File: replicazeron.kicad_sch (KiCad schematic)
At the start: 75 parts, among them J1 Conn_01x06_Male, J10 Conn_01x03_Pin, J2 Conn_01x06_Male, J3 Conn_01x06_Male, J4 Conn_01x06_Male, J5 Conn_01x06_Male, J6 Conn_01x05_Male, J7 Conn_01x05_Female, J8 Conn_01x06_Female, J9 Conn_01x04_Male, SW1 SW_Push, SW10 SW_Push, SW11 SW_Push, SW12 SW_Push, SW13 SW_Push, SW14 SW_Push, SW15 SW_Push, SW16 SW_Push, SW17 SW_Push, SW18 SW_Push, SW19 SW_Push, SW2 SW_Push, SW20 SW_Push, SW21 SW_Push, SW22 SW_Push, SW23 SW_Push, SW24 SW_Push, SW25 SW_Push, SW26 SW_Push, SW27 SW_Push, SW28 SW_Push, SW29 SW_Push, SW3 SW_Push, SW4 SW_Push, SW5 SW_Push, SW6 SW_Push, SW7 SW_Push, SW8 SW_Push, SW9 SW_Push, U1 STM32F103C8Tx

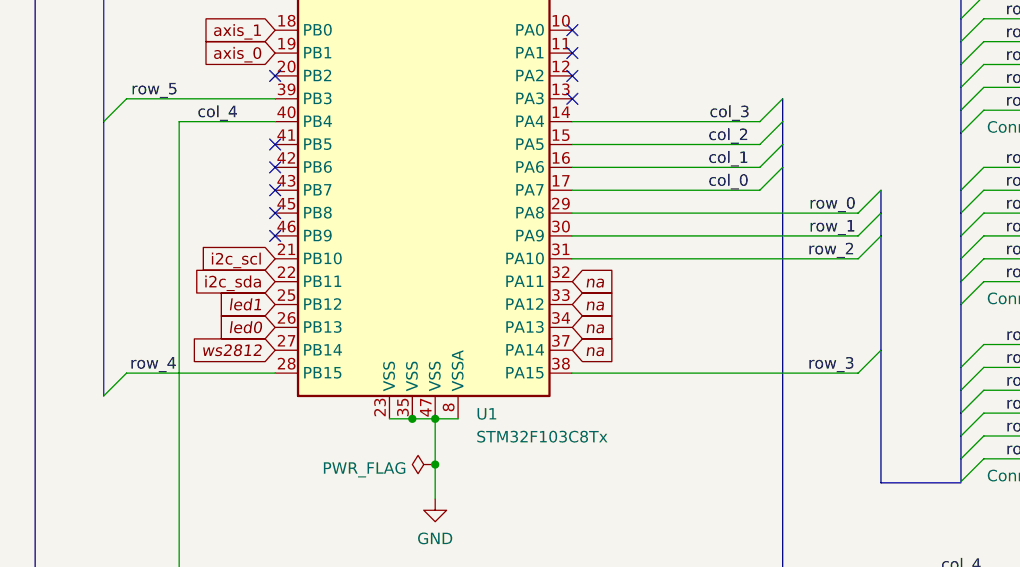
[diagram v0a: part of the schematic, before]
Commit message: fix row order
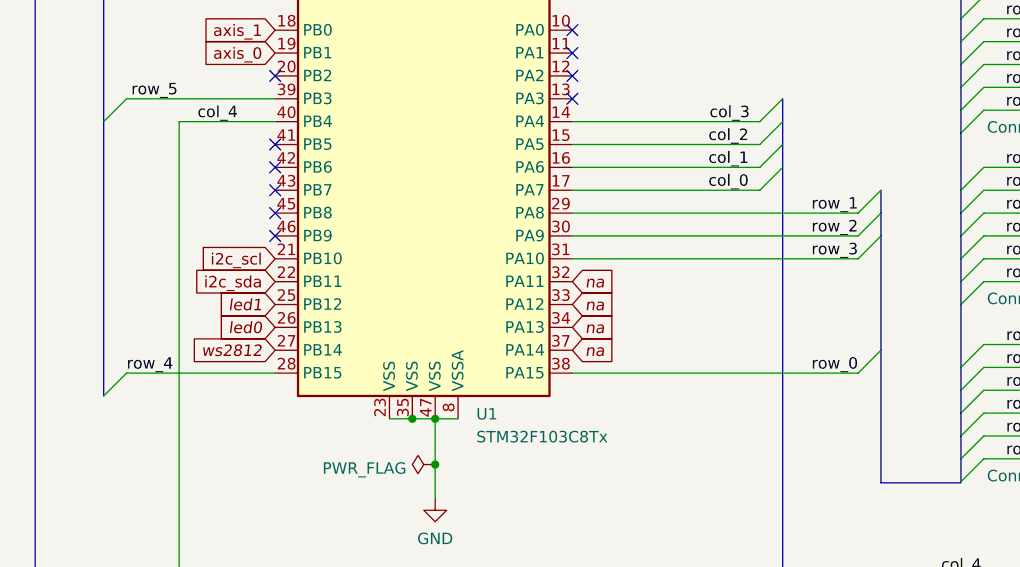
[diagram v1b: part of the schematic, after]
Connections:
- net row_0: now also U1.38 (PA15); no longer U1.29 (PA8)
- net row_1: now also U1.29 (PA8); no longer U1.30 (PA9)
- net row_2: now also U1.30 (PA9); no longer U1.31 (PA10)
- net row_3: now also U1.31 (PA10); no longer U1.38 (PA15)
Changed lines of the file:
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@@
 	)
 	(label "row_3"
-		(at 108.839 241.3 180)
+		(at 109.22 228.6 180)
 		(fields_autoplaced yes)
 		(effects
@@
 	)
 	(label "row_0"
-		(at 108.966 223.52 180)
+		(at 109.22 241.3 180)
 		(fields_autoplaced yes)
 		(effects
@@
 	)
 	(label "row_1"
-		(at 108.966 226.06 180)
+		(at 109.22 223.52 180)
 		(fields_autoplaced yes)
 		(effects
@@
 	)
 	(label "row_2"
-		(at 108.839 228.6 180)
+		(at 109.22 226.06 180)
 		(fields_autoplaced yes)
 		(effects
@@
 	)
 	(label "row_4"
-		(at 28.321 241.3 0)
-		(fields_autoplaced yes)
-		(effects
+		(at 27.94 241.3 0)
+		(fields_autoplaced yes)
+		(effects

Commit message: add missing switch: thumb_side; update components from library
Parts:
- removed D26, D27, D28, D29, D30, D31, D7: 1N4148, Diode_THT:D_DO-35_SOD27_P7.62mm_Horizontal, symbol Diode:1N4148
- removed J1, J2, J3, J4, J5: Conn_01x06_Male, Connector_PinSocket_2.54mm:PinSocket_1x06_P2.54mm_Vertical, symbol Connector:Conn_01x06_Male
- removed J6: Conn_01x05_Male, symbol Connector:Conn_01x05_Male
- removed J7: Conn_01x05_Female, symbol Connector:Conn_01x05_Female
- removed J8: Conn_01x06_Female, symbol Connector:Conn_01x06_Female
- removed J9: Conn_01x04_Male, Connector_PinSocket_2.54mm:PinSocket_1x06_P2.54mm_Vertical, symbol Connector:Conn_01x04_Male
- removed SW24, SW25, SW26, SW27, SW28, SW29, SW7: SW_Push, symbol Switch:SW_Push
- added D32, D33, D34, D35, D36, D37, D38, D39: 1N4148, Diode_THT:D_DO-35_SOD27_P7.62mm_Horizontal, symbol Diode:1N4148
- added J1, J2, J3, J4, J5: Conn_01x06_Pin, symbol Connector:Conn_01x06_Pin
- added J6: Conn_01x05_Pin, symbol Connector:Conn_01x05_Pin
- added J7: Conn_01x05_Socket, symbol Connector:Conn_01x05_Socket
- added J8: Conn_01x06_Socket, symbol Connector:Conn_01x06_Socket
- added J9: Conn_01x04_Pin, symbol Connector:Conn_01x04_Pin
- added SW30, SW31, SW32, SW33, SW34, SW35, SW36, SW37: SW_Push, symbol Switch:SW_Push
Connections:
- net +3V3 is gone; now on net +3.3V: RV1.1, RV2.1
- net GND: now also J9.1 (Pin_1)
- net col_0: now also J6.1 (Pin_1), J7.1 (Pin_1); no longer SW10.1, SW11.1, SW12.1, SW13.1, SW14.1, SW15.1, SW16.1, SW17.1, SW18.2, SW19.1, SW20.1, SW21.1, SW22.1, SW23.1, SW8.1, SW9.1, U1.14 (PA4), U1.15 (PA5), U1.16 (PA6)
- net col_4: now also J6.5 (Pin_5), J7.5 (Pin_5), SW32.2, SW33.1, SW34.1, SW35.1, SW36.1, SW37.1
- net i2c_scl: now also J9.3 (Pin_3)
- net i2c_sda: now also J9.2 (Pin_2)
- net row_0: now also D14.1 (K), D14.2 (A), D23.1 (K), D23.2 (A), D8.1 (K), D8.2 (A), SW12.2, SW19.2, D35.1 (K), D35.2 (A), J1.1 (Pin_1), J2.1 (Pin_1), J3.1 (Pin_1), J4.1 (Pin_1), J5.1 (Pin_1), J8.6 (Pin_6), SW31.2, SW37.2; no longer D12.1 (K), D12.2 (A), D21.1 (K), D21.2 (A), SW11.2, SW16.2, SW23.2
- net row_1: now also D15.1 (K), D24.1 (K), D9.1 (K), D36.1 (K), J1.2 (Pin_2), J2.2 (Pin_2), J3.2 (Pin_2), J4.2 (Pin_2), J5.2 (Pin_2), J8.5 (Pin_5); no longer D13.1 (K), D22.1 (K), D8.1 (K)
- net row_2: now also D10.1 (K), D16.1 (K), D25.1 (K), D37.1 (K), J1.3 (Pin_3), J2.3 (Pin_3), J3.3 (Pin_3), J4.3 (Pin_3), J5.3 (Pin_3), J8.4 (Pin_4); no longer D14.1 (K), D23.1 (K), D9.1 (K)
- net row_3: now also D11.1 (K), D18.1 (K), D32.1 (K), D38.1 (K), J1.4 (Pin_4), J2.4 (Pin_4), J3.4 (Pin_4), J4.4 (Pin_4), J5.4 (Pin_4), J8.3 (Pin_3); no longer D10.1 (K), D15.1 (K), D24.1 (K)
- net row_4: now also D12.1 (K), D21.1 (K), D33.1 (K), D39.1 (K), J1.5 (Pin_5), J2.5 (Pin_5), J3.5 (Pin_5), J4.5 (Pin_5), J5.5 (Pin_5), J8.2 (Pin_2); no longer D11.1 (K), D16.1 (K), D25.1 (K)
- net row_5: now also D13.1 (K), D22.1 (K), D34.1 (K), J1.6 (Pin_6), J2.6 (Pin_6), J3.6 (Pin_6), J4.6 (Pin_6), J5.6 (Pin_6), J8.1 (Pin_1); no longer D18.1 (K)
- net at SW14.2: now also D21.2 (A); no longer D14.2 (A)
- net at SW10.2: now also D10.2 (A); no longer D8.2 (A)
- net at SW21.2: now also D33.2 (A); no longer D23.2 (A)
- net +3.3V: now reaches R1.2, R2.2
- net +3.3V: now also J9.4 (Pin_4)
- net at D9.2 (A): now also SW11.2; no longer SW9.2
- net at SW22.2: now also D32.2 (A); no longer D22.2 (A)
- net at D11.2 (A): now also SW9.2
- net at D24.2 (A): now also SW30.2; no longer SW20.2
- net at D25.2 (A): now also SW23.2; no longer SW19.2
- net at D13.2 (A): now also SW13.1; no longer SW15.2
- net at D16.2 (A): now also SW16.2; no longer SW12.2
- net at D18.2 (A): now also SW15.2; no longer SW18.1
- net at D15.2 (A): now also SW18.2; no longer SW13.2
- net at SW8.2: now also D12.2 (A); no longer D10.2 (A)
- new net: D22.2 (A), SW20.1
- new net: D37.2 (A), SW35.2
- new net: D38.2 (A), SW34.2
- new net: D36.2 (A), SW36.2
- new net: D34.2 (A), SW32.1
- new net: D39.2 (A), SW33.2
- new net col_1: J6.2 (Pin_2), J7.2 (Pin_2), SW10.1, SW11.1, SW12.1, SW17.1, SW8.1, SW9.1, U1.16 (PA6)
- new net col_2: J6.3 (Pin_3), J7.3 (Pin_3), SW13.2, SW14.1, SW15.1, SW16.1, SW18.1, SW19.1, U1.15 (PA5)
- new net col_3: J6.4 (Pin_4), J7.4 (Pin_4), SW20.2, SW21.1, SW22.1, SW23.1, SW30.1, SW31.1, U1.14 (PA4)
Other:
- note added: "AnalogStick_Click"
- note added: "SideButtonLeft"
- note added: "SideButtonRight"
- note added: "SideButtonThumb"
- moved on the sheet: D1, D17, D2, D3, D4, D5, D6, RV1, RV2, SW1, SW17, SW2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
